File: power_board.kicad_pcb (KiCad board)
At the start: 2 copper layers, 64.8 x 52.1 mm, 40 parts, among them J1 RasPi_Conn2x20, J2 Power Supply, J3 MuddPi Conn, J4 LED Conn, Q1 Q_NMOS_DGS, Q10 Q_NMOS_DGS, Q11 Q_NMOS_DGS, Q12 Q_NMOS_DGS, Q13 Q_PMOS_DGS, Q14 Q_PMOS_DGS, Q15 Q_PMOS_DGS, Q16 Q_PMOS_DGS, Q17 Q_NMOS_DGS, Q18 Q_NMOS_DGS, Q19 Q_NMOS_DGS, Q2 Q_NMOS_DGS, Q20 Q_NMOS_DGS, Q21 Q_PMOS_DGS, Q22 Q_PMOS_DGS, Q23 Q_PMOS_DGS, Q24 Q_PMOS_DGS, Q3 Q_NMOS_DGS, Q4 Q_NMOS_DGS, Q5 Q_PMOS_DGS, Q6 Q_PMOS_DGS, Q7 Q_PMOS_DGS, Q8 Q_PMOS_DGS, Q9 Q_NMOS_DGS

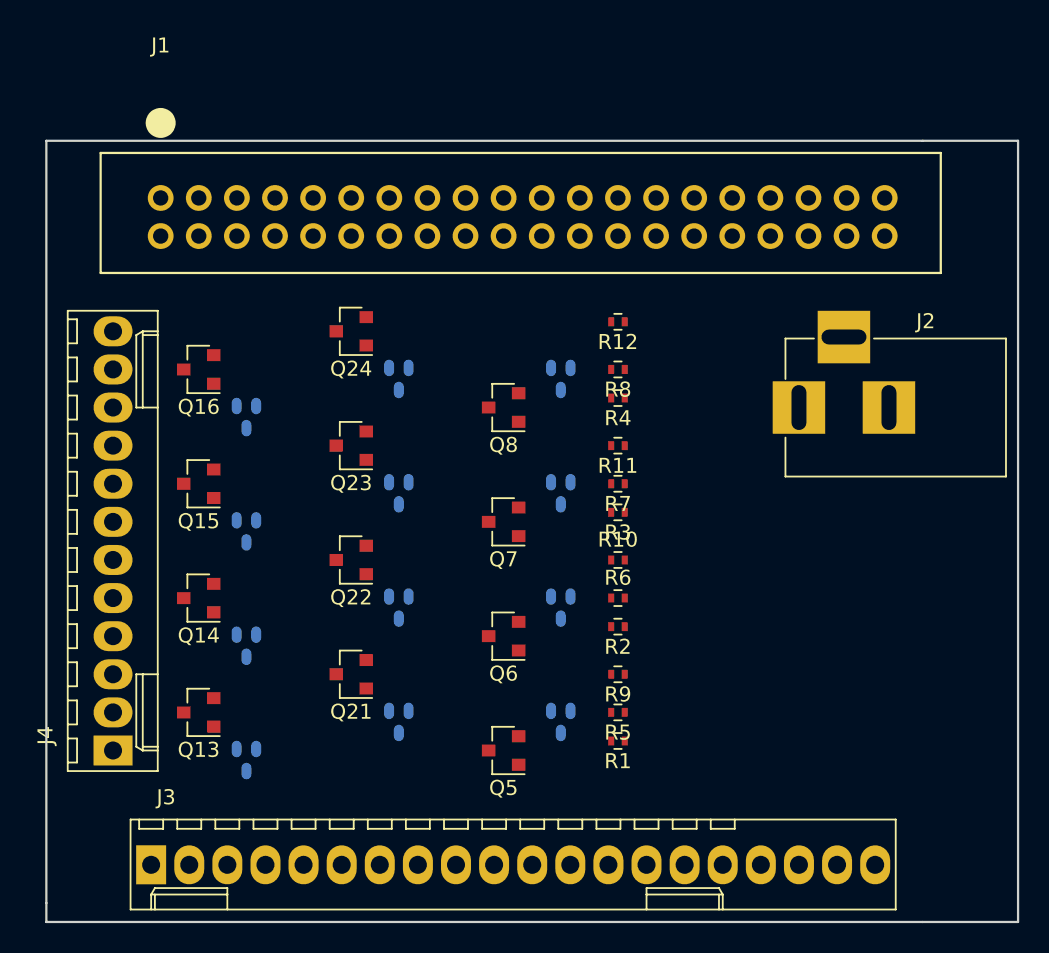
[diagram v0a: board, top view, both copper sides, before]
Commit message: Fixed some issues with the layout and made it conform to the OSH Park manufacturing specifications.  Ordered the board!!!
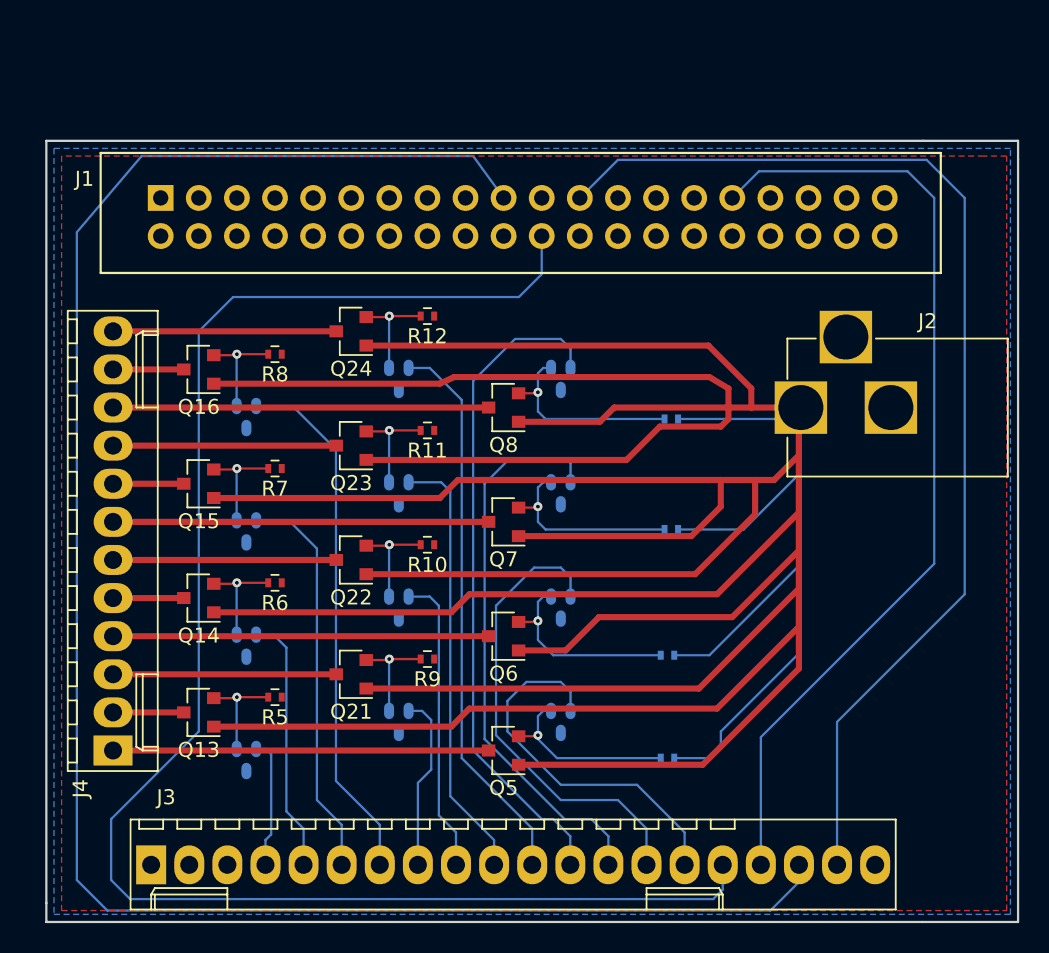
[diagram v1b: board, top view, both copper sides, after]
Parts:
- J2: footprint Connect:BARREL_JACK -> wall:BARREL_JACK
- R1, R2, R3, R4: moved to B.Cu
- moved R5 22.9 mm to (96.5, 87.9)
- moved R6 22.9 mm to (96.5, 80.3), turned to 180 degrees
- moved R7 22.9 mm to (96.5, 72.6)
- moved R8 22.9 mm to (96.5, 65.0)
- moved R10 12.7 mm to (106.7, 77.7), turned to 180 degrees
- moved R11 12.7 mm to (106.7, 70.1)
- moved R9 12.7 mm to (106.7, 85.3)
- moved R12 12.7 mm to (106.7, 62.5)
- moved R4 3.82 mm to (122.9, 69.3)
- moved R2 3.81 mm to (122.7, 85.1)
- moved R3 3.74 mm to (122.9, 76.7)
- moved R1 3.49 mm to (122.7, 91.9)
- moved J2 0.13 mm to (131.6, 68.6)
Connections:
- J3 pad 12: R_Control_1 -> R_Control_4
- J3 pad 13: R_Control_2 -> R_Control_3
- J3 pad 14: R_Control_3 -> R_Control_2
- J3 pad 15: R_Control_4 -> R_Control_1
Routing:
- net +5V: track 0.00 -> 443.8 mm
- net MOSI: track 0.00 -> 126.3 mm
- net isBeat: track 0.00 -> 109.2 mm
- net SCLK: track 0.00 -> 75.7 mm
- net color: track 0.00 -> 64.2 mm
- net R_Control_4: track 0.00 -> 44.6 mm
- net R_Control_3: track 0.00 -> 37.6 mm
- net B_Control_4: track 0.00 -> 37.4 mm
- net G_Control_4: track 0.00 -> 35.4 mm
- net R_Control_2: track 0.00 -> 31.2 mm
- net B_Control_3: track 0.00 -> 29.1 mm
- net G_Control_3: track 0.00 -> 26.6 mm
- net R_Control_1: track 0.00 -> 25.1 mm
- net R4: track 0.00 -> 25.0 mm
- net R3: track 0.00 -> 25.0 mm
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- added copper zone on F.Cu, net +5V
- added copper zone on B.Cu, net GND
